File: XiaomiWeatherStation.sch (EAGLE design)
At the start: 0 parts

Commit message: Adds components to schematic file
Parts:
- added IC1: (no value), SSFD - ESP32 WEMOS LOLIN CHINA W_BATT:SSFD_LOLIN32_WEMOS_CHINA_W_BATT
- added JP1, JP2: (no value), pinhead:PINHD-1X4
- added JP3: (no value), pinhead:PINHD-1X2
- added MOD1: CARD-SD-ADAPTER-CATALEX, SD-Card-Module_CATALEX:CARD-SD-ADAPTER-CATALEX
- added U$1: SIM800LMODULE, SIM800LMODULE:SIM800LMODULE
- added U$2: RTC-DS3231-AT24C32, diy-modules:RTC-DS3231-AT24C32
- added U$3: DC-DC-STEP-DOWN-LM2596, diy-modules:DC-DC-STEP-DOWN-LM2596
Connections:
- new net 3V7: U$1.VCC, U$3.OUT+
- new net 5V: IC1.5V, JP1.2, JP2.2, MOD1.5V
- new net GND: IC1.GNDA, JP1.1, JP2.1, MOD1.GND, U$1.GND, U$3.OUT-
- new net MISO: IC1.19, MOD1.MISO
- new net MOSI: IC1.23, MOD1.MOSI
- new net N$1: JP3.2, U$3.IN+
- new net N$2: JP3.1, U$3.IN-
- new net RXD2: IC1.16, U$1.TX
- new net SCK: IC1.18, MOD1.SCK
- new net SCL: IC1.22, JP1.4, JP2.4
- new net SDA: IC1.21, JP1.3, JP2.3
- new net SS: IC1.5, MOD1.CS
- new net TXD2: IC1.17, U$1.RX

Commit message: Finish routing
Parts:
- removed U$2: RTC-DS3231-AT24C32, diy-modules:RTC-DS3231-AT24C32
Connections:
- net N$1 renamed IN+
- net N$2 renamed IN-
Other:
- moved on the sheet: IC1, JP1, JP2, JP3, MOD1, U$3

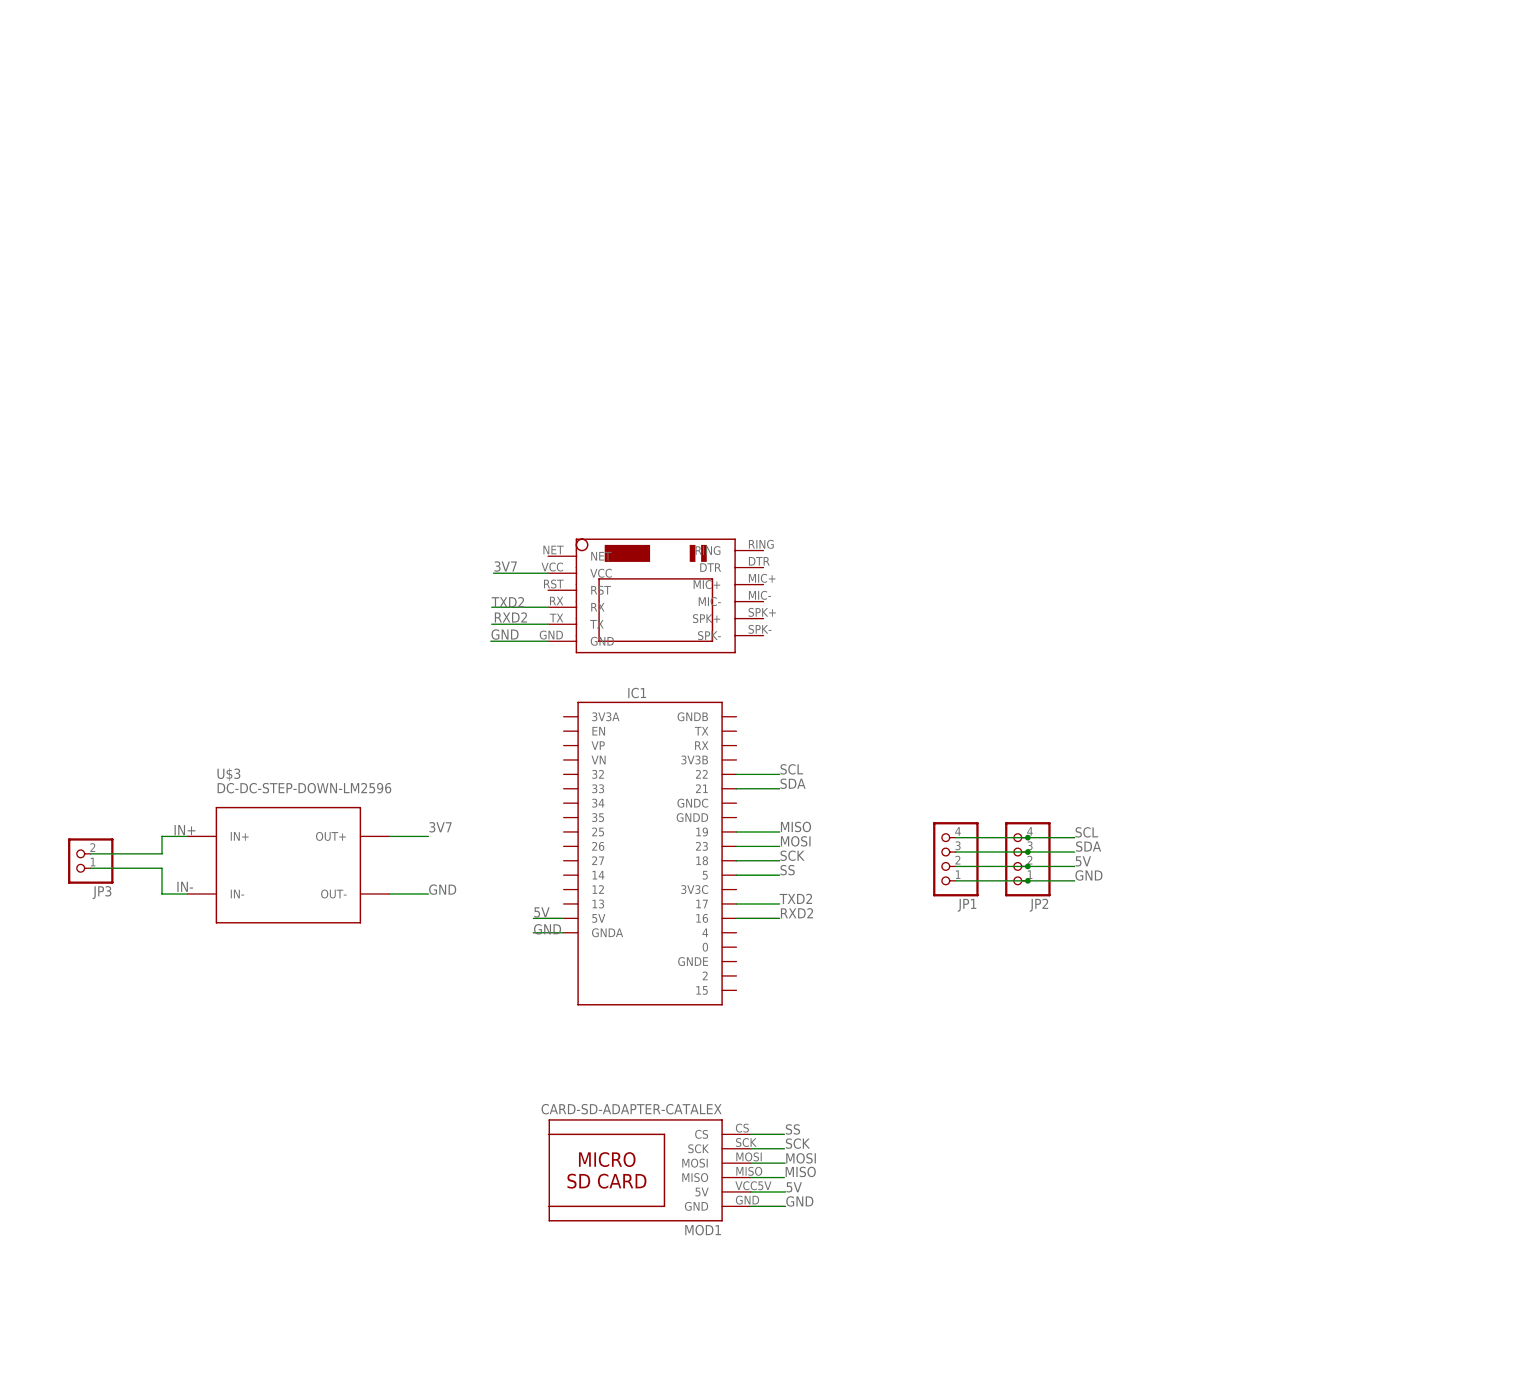
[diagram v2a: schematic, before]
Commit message: Adds relay to the schematic
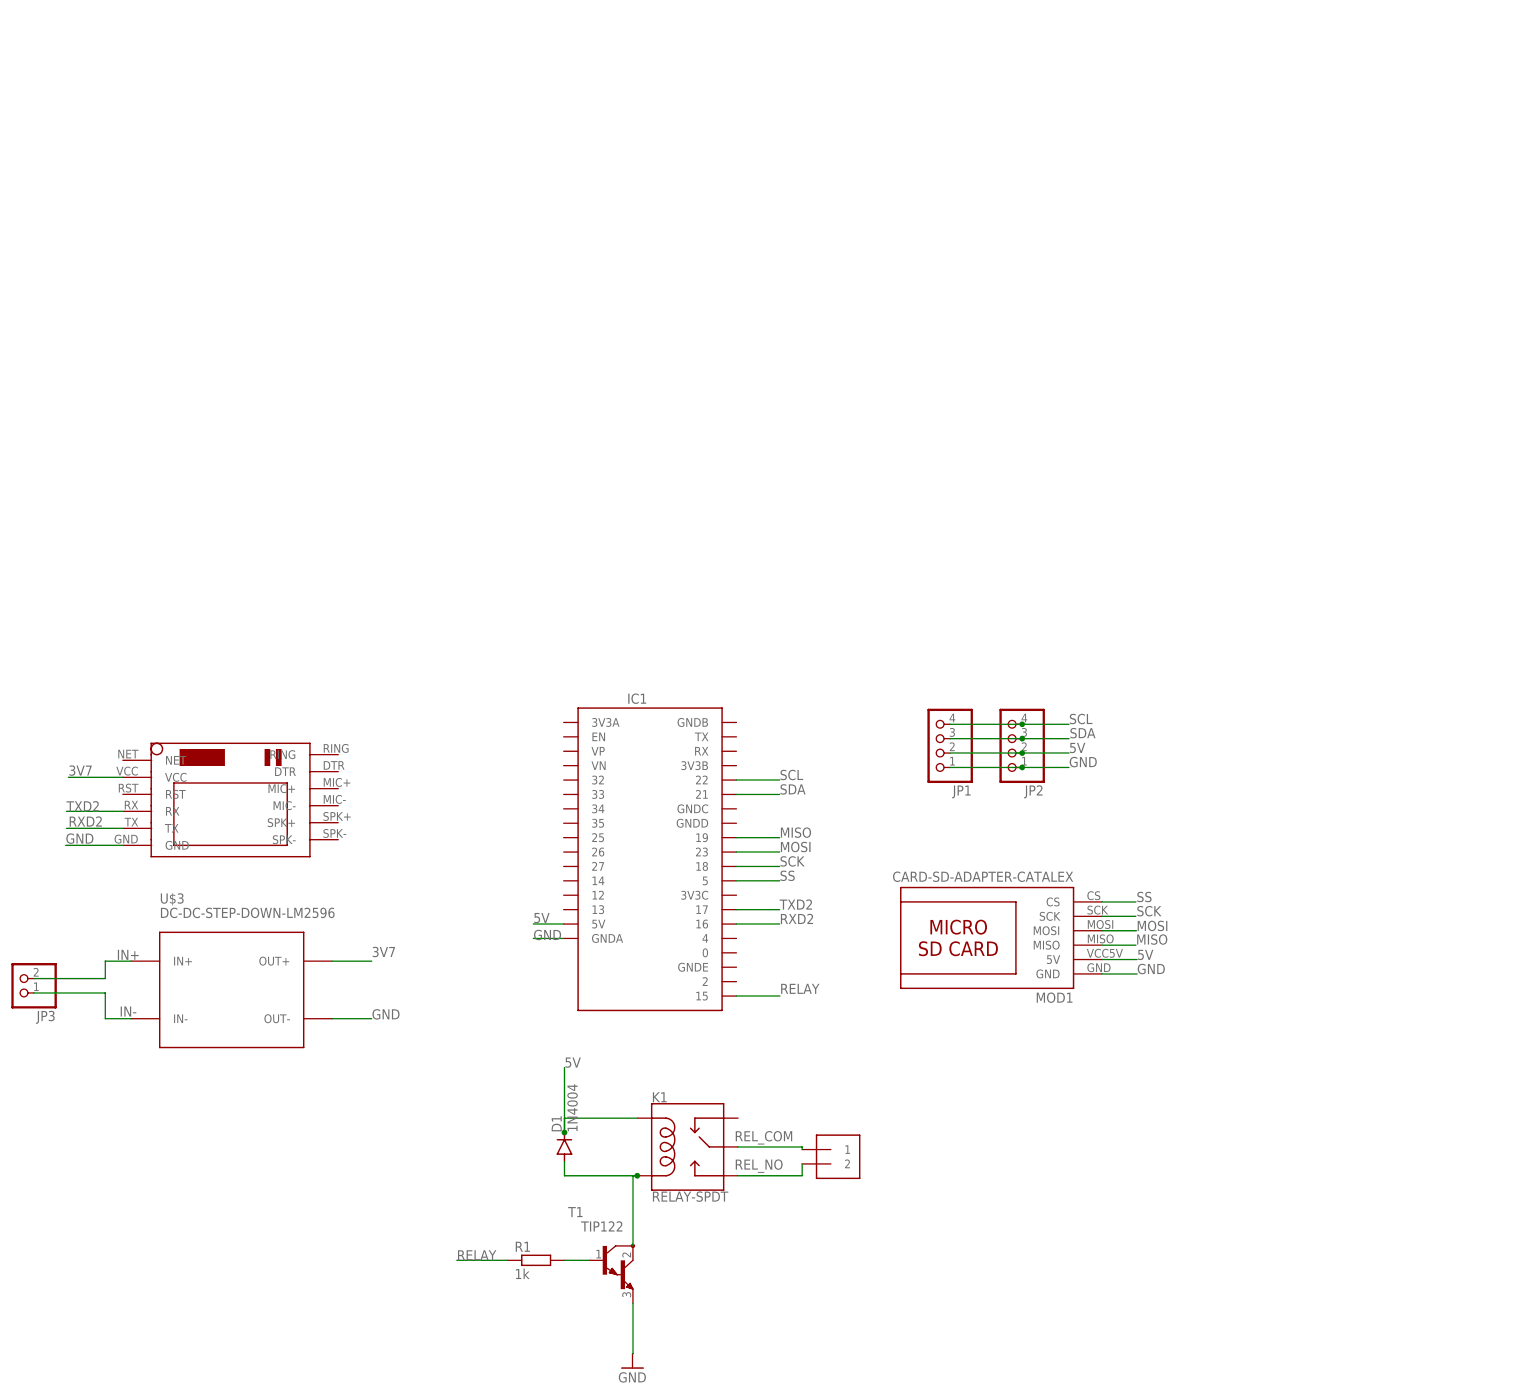
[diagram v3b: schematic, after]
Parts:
- added D1: 1N4004, diode:1N4004
- added J1: 1X2-3.5MM, adafruit:1X2-3.5MM
- added K1: RELAY-SPDT, SparkFun-Electromechanical:RELAY-SPDT
- added R1: 1k, rcl:R-EU_0204/7
- added T1: TIP122, transistor:TIP122
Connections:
- new net N$1: R1.2, T1.B
- new net N$2: D1.A, K1.COIL2, T1.C
- new net RELAY: IC1.15, R1.1
- new net REL_COM: J1.1, K1.MAIN
- new net REL_NO: J1.2, K1.NO
- net 5V: now also D1.C, K1.COIL1
- net GND: now also T1.E
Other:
- moved on the sheet: IC1, JP1, JP2, JP3, MOD1, U$3

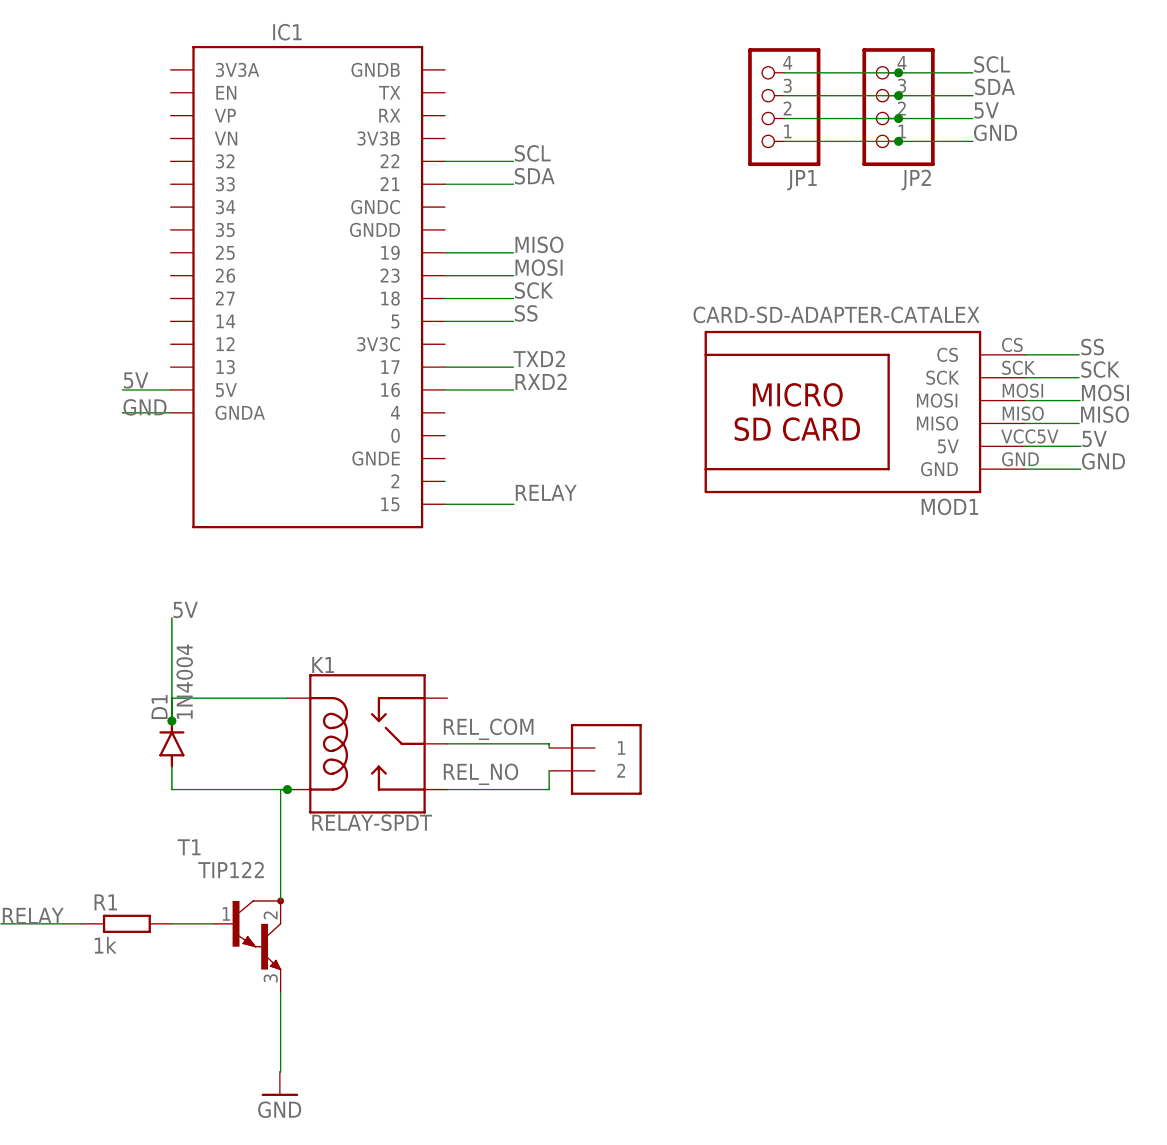
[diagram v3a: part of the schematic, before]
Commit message: Completes routing
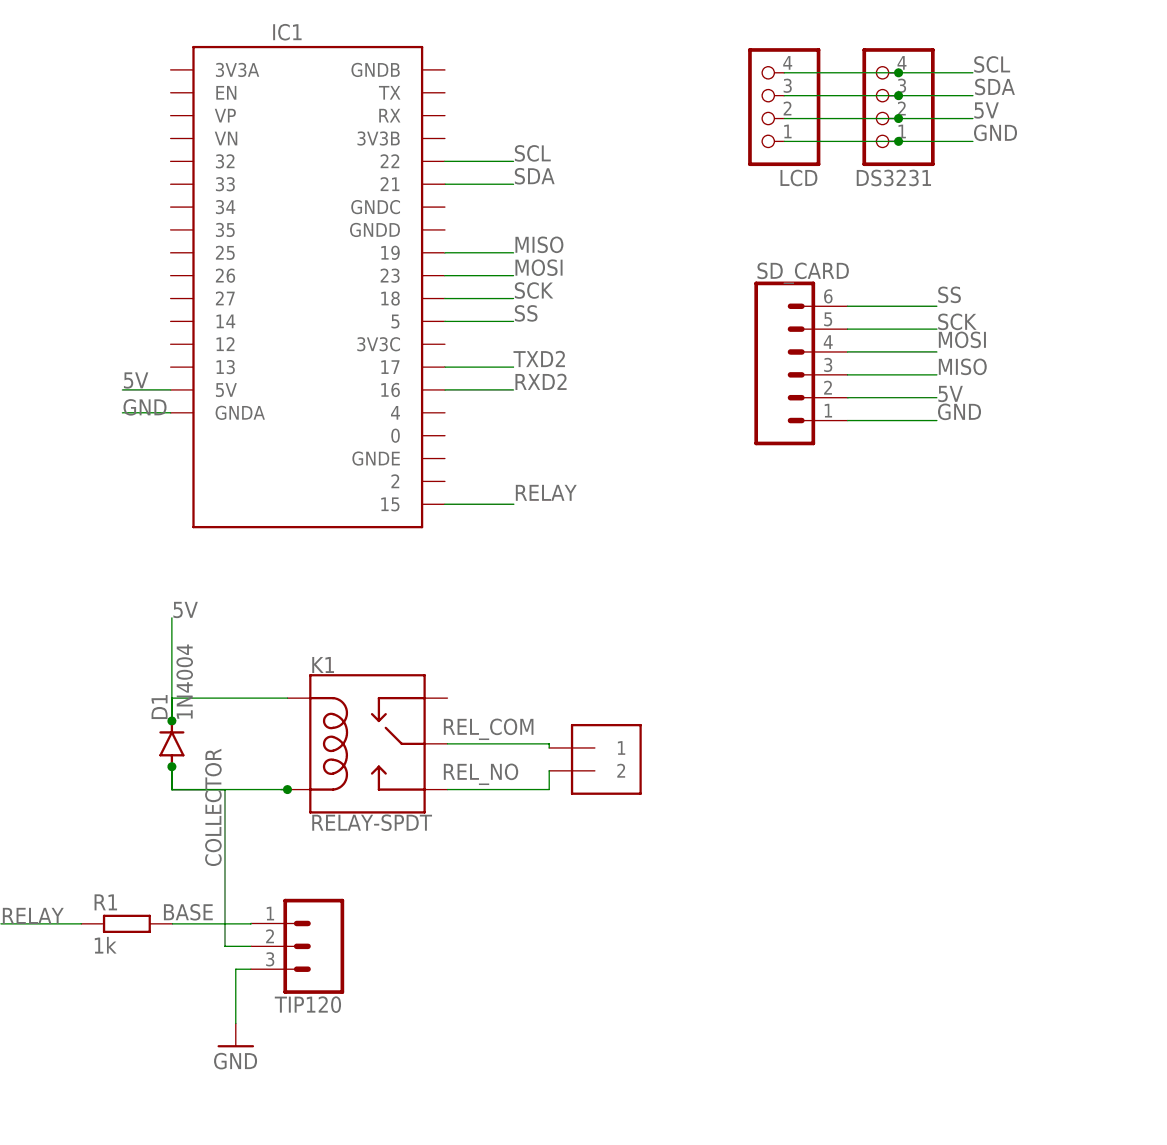
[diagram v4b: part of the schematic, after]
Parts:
- removed MOD1: CARD-SD-ADAPTER-CATALEX, SD-Card-Module_CATALEX:CARD-SD-ADAPTER-CATALEX
- removed T1: TIP122, transistor:TIP122
- added SD_CARD: (no value), SparkFun-Connectors:CONN_06LONGPADS
- added TIP120: (no value), SparkFun-Connectors:CONN_03LONGPADS
- renumbered JP1 to LCD, JP2 to DS3231
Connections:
- removed net N$1: R1.2, T1.B
- removed net N$2: D1.A, K1.COIL2, T1.C
- new net BASE: R1.2, TIP120.1
- new net COLLECTOR: D1.A, K1.COIL2, TIP120.2
- net 5V: now also SD_CARD.2; no longer MOD1.5V
- net GND: now also SD_CARD.1, TIP120.3; no longer MOD1.GND, T1.E
- net MISO: now also SD_CARD.3; no longer MOD1.MISO
- net MOSI: now also SD_CARD.4; no longer MOD1.MOSI
- net SCK: now also SD_CARD.5; no longer MOD1.SCK
- net SS: now also SD_CARD.6; no longer MOD1.CS
